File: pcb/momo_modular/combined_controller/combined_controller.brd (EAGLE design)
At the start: 50.8 x 33 mm, 44 parts, among them Q2 P-MOSFET, U1 XRP7659, U2 PIC24FJ64GA306, U3 MCP1702, U5 FLASH8MSOP8, U6 MCP73811

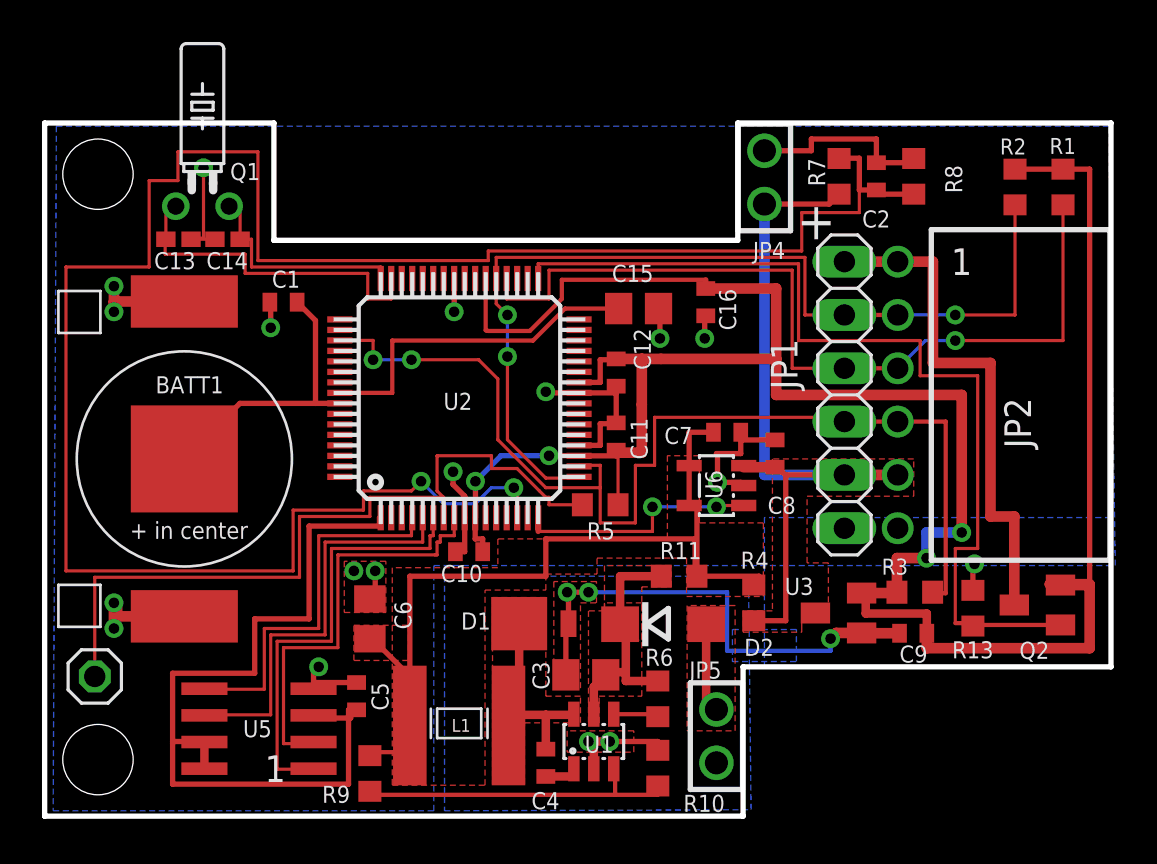
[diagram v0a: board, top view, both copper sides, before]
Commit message: Finalize combined controller layout
- Switch power connector to one that doesn't require a board cutout
- Relay out traces better given that we note have more space
- Make the board a regular shape
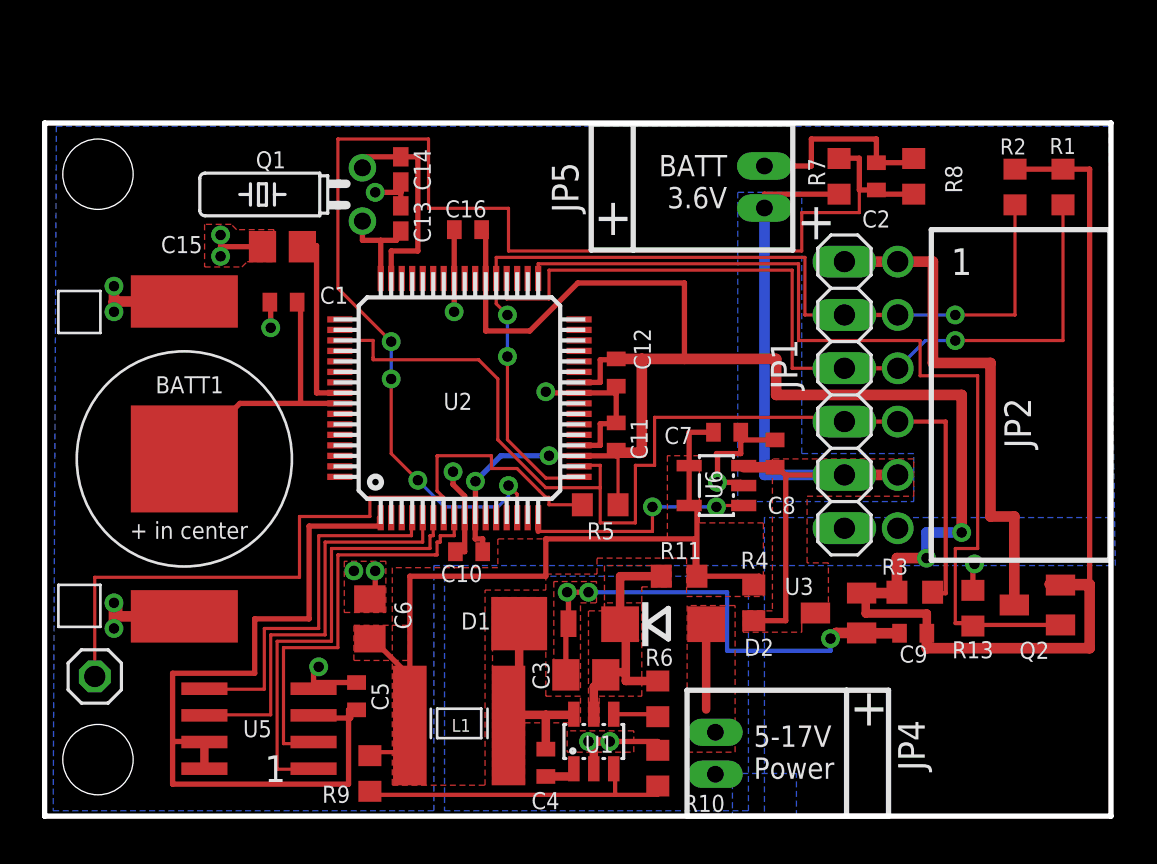
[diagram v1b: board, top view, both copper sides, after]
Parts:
- JP4, JP5: value MOMO-EDGE-POWER-M -> MOMO-PWR-HOUSED; device components:MOMO-EDGE-SMALL-2M -> components:MOMO-PWR-HOUSED
- moved JP4 27.5 mm to (66.0, 14.9), turned to 270 degrees
- moved JP5 26.3 mm to (68.3, 41.9), turned to 90 degrees
- moved C15 17.2 mm to (45.4, 39.1), turned to 180 degrees
- moved C16 11.8 mm to (54.2, 39.9), turned to 180 degrees
- moved C13 10.6 mm to (51.0, 40.4), turned to 90 degrees
- moved C14 8.90 mm to (51.0, 42.7), turned to 270 degrees
- moved Q1 7.64 mm to (49.2, 41.6), turned to 90 degrees
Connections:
- net +18V: now also JP4.1; no longer JP5.2
- net GND: now also JP4.2, JP5.2; no longer JP4.1, JP5.1
- net N$6: now also U2.47; no longer U2.48
- net N$7: now also U2.48; no longer U2.47
- net V+: now also JP5.1; no longer JP4.2
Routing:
- net VBAT_SAMP: track 99.3 -> 63.5 mm, vias 2 -> 4
- net N$7: track 16.7 -> 4.87 mm
- net VCAP: track 16.4 -> 8.85 mm
- net VCCINT: track 119.9 -> 117.2 mm
- net GND: track 85.4 -> 84.9 mm
- net N$6: track 10.7 -> 10.2 mm
- net IRQ: vias 2 -> 0
- added copper zone on layer 16, net V+
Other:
- outline, holes or cut-outs redrawn
- board text added: "5-17V Power"
- board text added: "BATT 3.6V"
